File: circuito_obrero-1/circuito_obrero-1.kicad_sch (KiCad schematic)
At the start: 41 parts, among them J1 Conn_01x03_Pin, J10 Conn_01x05, J2 Conn_01x03_Pin, J3 Conn_01x03_Pin, J4 Conn_01x03_Pin, J5 Conn_01x03_Pin, J6 Conn_01x03_Pin, J7 Conn_01x03_Pin, J8 Conn_01x03_Pin, J9 Conn_01x05, U1 74HC165, U2 74HC165, U3 74HC165

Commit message: pre añadir lagrimas
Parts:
- removed H_A_j3_pin3, H_B_j3_pin3: MountingHole_Pad, MountingHole:MountingHole_2.2mm_M2_DIN965_Pad_TopOnly, symbol Mechanical:MountingHole_Pad
- added PUENTE_1, PUENTE_2, PUENTE_3, PUENTE_4, PUENTE_7, PUENTE_9: 0k, Resistor_THT:R_Axial_DIN0204_L3.6mm_D1.6mm_P7.62mm_Horizontal, symbol Device:R
- added PUENTE_5: 0k, Resistor_THT:R_Axial_DIN0207_L6.3mm_D2.5mm_P15.24mm_Horizontal, symbol Device:R
- added PUENTE_6, PUENTE_8: 0k, Resistor_THT:R_Axial_DIN0207_L6.3mm_D2.5mm_P10.16mm_Horizontal, symbol Device:R
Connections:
- net GND: now also PUENTE_6.1, PUENTE_6.2, PUENTE_7.1, PUENTE_7.2, PUENTE_8.1, PUENTE_8.2
- net VCC: now also PUENTE_9.1, PUENTE_9.2
- net at J2.1 (Pin_1), R4.2, U1.14 (D3): now also PUENTE_1.1, PUENTE_1.2
- net at J10.1 (Pin_1), J9.1 (Pin_1), U1.1 (~{PL})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: now also PUENTE_2.1, PUENTE_2.2, PUENTE_4.1, PUENTE_4.2
- net at U2.9 (Q7), U3.10 (DS): now also PUENTE_5.1, PUENTE_5.2
- net at U1.9 (Q7), U2.10 (DS): now also PUENTE_3.1, PUENTE_3.2
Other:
- moved on the sheet: H5_A_j8_pin1, R4, R9

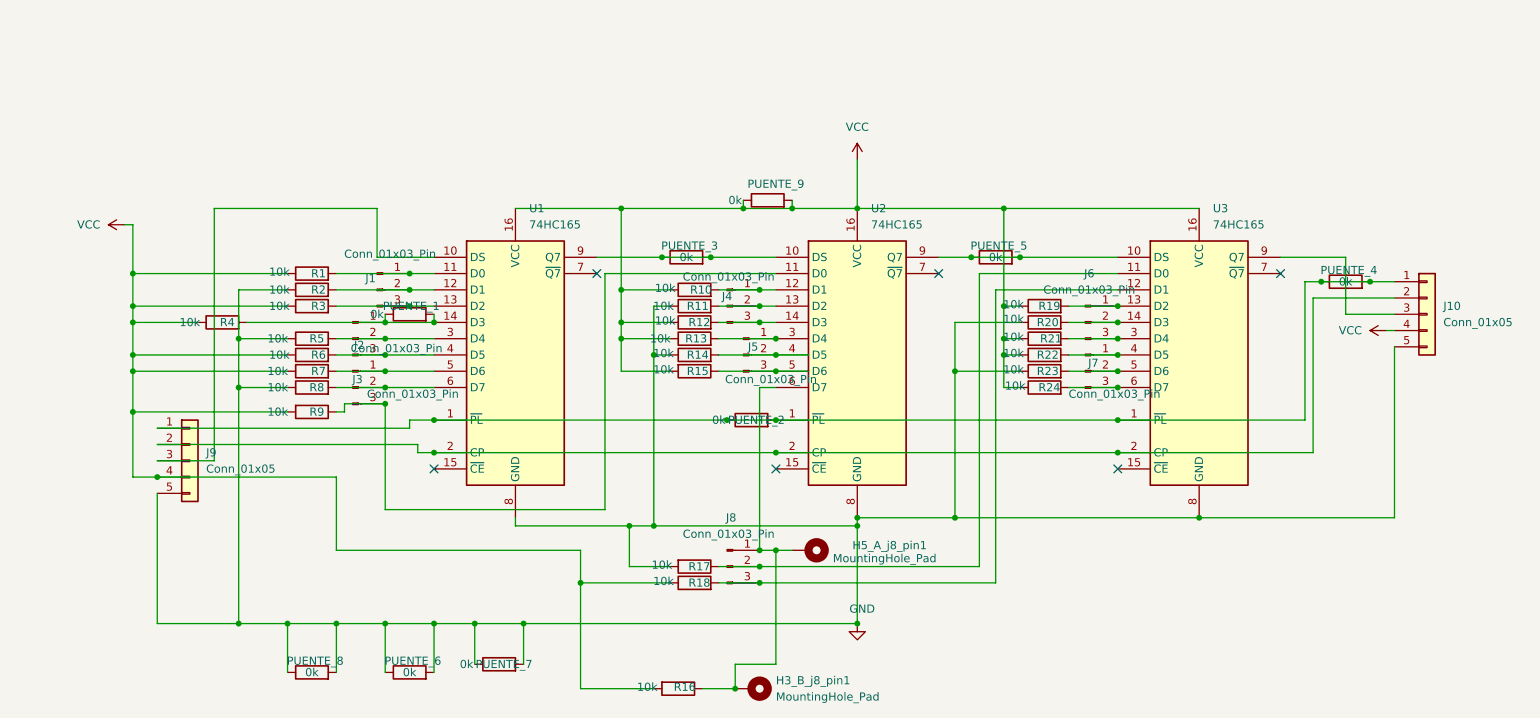
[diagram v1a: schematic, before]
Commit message: redo de circuito 2 chip x 4 encoder
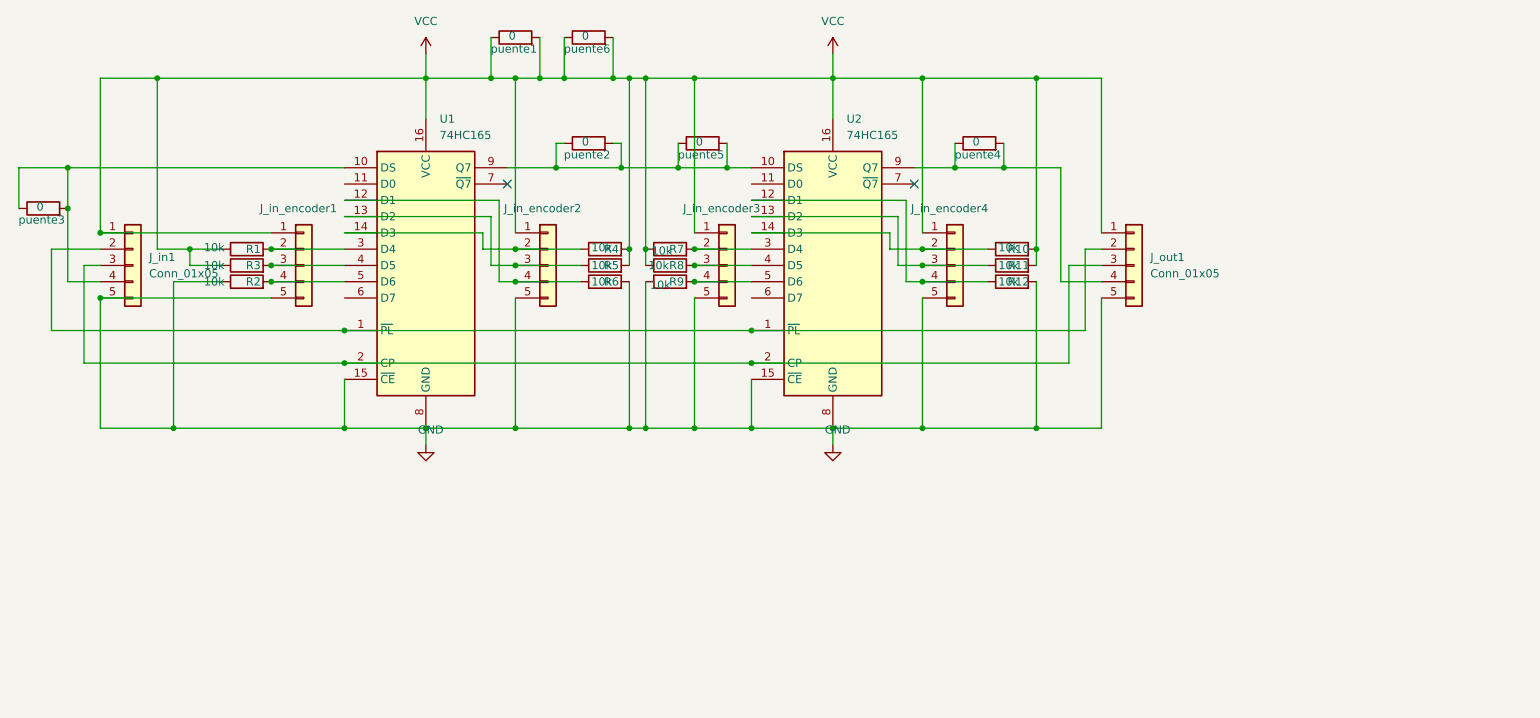
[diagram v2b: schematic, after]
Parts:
- removed H3_B_j8_pin1, H5_A_j8_pin1: MountingHole_Pad, MountingHole:MountingHole_2.2mm_M2_DIN965_Pad_TopOnly, symbol Mechanical:MountingHole_Pad
- removed J1, J2, J3, J4, J5, J6, J7, J8: Conn_01x03_Pin, Connector_JST:JST_EH_B3B-EH-A_1x03_P2.50mm_Vertical, symbol Connector:Conn_01x03_Pin
- removed PUENTE_1, PUENTE_2, PUENTE_3, PUENTE_4, PUENTE_7, PUENTE_9: 0k, Resistor_THT:R_Axial_DIN0204_L3.6mm_D1.6mm_P7.62mm_Horizontal, symbol Device:R
- removed PUENTE_5: 0k, Resistor_THT:R_Axial_DIN0207_L6.3mm_D2.5mm_P15.24mm_Horizontal, symbol Device:R
- removed PUENTE_6, PUENTE_8: 0k, Resistor_THT:R_Axial_DIN0207_L6.3mm_D2.5mm_P10.16mm_Horizontal, symbol Device:R
- removed R13, R14, R15, R16, R17, R18, R19, R20, R21, R22, R23, R24: 10k, Resistor_THT:R_Axial_DIN0204_L3.6mm_D1.6mm_P7.62mm_Horizontal, symbol Device:R
- removed U3: 74HC165, Package_DIP:CERDIP-16_W7.62mm_SideBrazed_LongPads_Socket, symbol 74xx:74HC165
- added J_in_encoder1, J_in_encoder2, J_in_encoder3, J_in_encoder4: Conn_01x05, Connector_JST:JST_EH_B5B-EH-A_1x05_P2.50mm_Vertical, symbol Connector_Generic:Conn_01x05
- added puente1, puente2, puente3, puente4, puente5, puente6: 0, Resistor_THT:R_Axial_DIN0204_L3.6mm_D1.6mm_P7.62mm_Horizontal, symbol Device:R
- renumbered J9 to J_in1, J10 to J_out1
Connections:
- net GND: now also R12.2, R6.2, R9.1, U1.15 (~{CE}), U2.15 (~{CE}), J_in_encoder1.5 (Pin_5), J_in_encoder2.5 (Pin_5), J_in_encoder3.5 (Pin_5), J_in_encoder4.5 (Pin_5); no longer R11.1, R5.1, R8.1
- net VCC: now also J_in1.1 (Pin_1), J_out1.1 (Pin_1), R10.2, R11.2, R4.2, R5.2, R8.1, J_in_encoder1.1 (Pin_1), J_in_encoder2.1 (Pin_1), J_in_encoder3.1 (Pin_1), J_in_encoder4.1 (Pin_1), puente1.1, puente1.2, puente6.1, puente6.2; no longer J_in1.4 (Pin_4), J_out1.4 (Pin_4), R10.1, R12.1, R4.1, R6.1, R9.2
- net at U2.5 (D6): now also R9.2, J_in_encoder3.4 (Pin_4)
- net at U1.13 (D2): now also R5.1, J_in_encoder2.3 (Pin_3); no longer R3.2
- net at U2.12 (D1): now also R12.1, J_in_encoder4.4 (Pin_4); no longer R10.2
- net at U2.9 (Q7): now also J_out1.4 (Pin_4), puente4.1, puente4.2
- net at R7.2: now also U2.3 (D4), J_in_encoder3.2 (Pin_2); no longer U1.5 (D6)
- net at R8.2: now also U2.4 (D5), J_in_encoder3.3 (Pin_3); no longer U1.6 (D7)
- net at U2.11 (D0): no longer R9.1
- net at R1.2: now also U1.3 (D4), J_in_encoder1.2 (Pin_2); no longer U1.11 (D0)
- net at U1.12 (D1): now also R6.1, J_in_encoder2.4 (Pin_4); no longer R2.2
- net at U1.14 (D3): now also R4.1, J_in_encoder2.2 (Pin_2); no longer R4.2
- net at U1.4 (D5): now also R3.2, J_in_encoder1.3 (Pin_3); no longer R6.2
- net at U1.1 (~{PL}), U2.1 (~{PL}): now also J_in1.2 (Pin_2), J_out1.2 (Pin_2); no longer J_in1.1 (Pin_1), J_out1.1 (Pin_1)
- net at U1.2 (CP), U2.2 (CP): now also J_in1.3 (Pin_3), J_out1.3 (Pin_3); no longer J_in1.2 (Pin_2), J_out1.2 (Pin_2)
- net at U1.9 (Q7), U2.10 (DS): now also puente2.1, puente2.2, puente5.1, puente5.2
- net at U2.14 (D3): now also R10.1, J_in_encoder4.2 (Pin_2); no longer R12.2
- net at U1.10 (DS): now also J_in1.4 (Pin_4), puente3.1, puente3.2; no longer J_in1.3 (Pin_3)
- net at U2.13 (D2): now also R11.1, J_in_encoder4.3 (Pin_3); no longer R11.2
- new net: J_in_encoder1.4 (Pin_4), R2.2, U1.5 (D6)
- no-connect marks 6 -> 2
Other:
- moved on the sheet: J_in1, J_out1, R1, R2, R3, U1

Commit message: circuito doble impresoin manual
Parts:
- added H1, H2, H3, H4: MountingHole, MountingHole:MountingHole_3.2mm_M3_DIN965, symbol Mechanical:MountingHole

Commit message: pines sueltos a gnd
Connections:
- net GND: now also U1.11 (D0), U1.6 (D7), U2.11 (D0), U2.6 (D7)
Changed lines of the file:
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@@
+	)
+	(junction
+		(at 71.12 109.22)
+		(diameter 0)
+		(color 0 0 0 0)
 	)
 	(junction
@@
 	)
 	(junction
+		(at 125.73 109.22)
+		(diameter 0)
+		(color 0 0 0 0)
+	)
+	(junction
 		(at 182.88 54.61)
 		(diameter 0)
@@
 	)
 	(junction
+		(at 133.35 109.22)
+		(diameter 0)
+		(color 0 0 0 0)
+	)
+	(junction
 		(at 138.43 93.98)
 		(diameter 0)
@@
 	(junction
 		(at 129.54 86.36)
+		(diameter 0)
+		(color 0 0 0 0)
+	)
+	(junction
+		(at 52.07 109.22)
 		(diameter 0)
 		(color 0 0 0 0)
@@
 	(wire
 		(pts
+			(xy 71.12 109.22) (xy 74.93 109.22)
+		)
+		(stroke
+			(width 0)
+			(type default)
+		)
+	)
+	(wire
+		(pts
 			(xy 45.72 54.61) (xy 87.63 54.61)
 		)
@@
 	(wire
 		(pts
+			(xy 71.12 88.9) (xy 71.12 109.22)
+		)
+		(stroke
+			(width 0)
+			(type default)
+		)
+	)
+	(wire
+		(pts
 			(xy 74.93 73.66) (xy 99.06 73.66)
 		)
@@
 	(wire
 		(pts
-			(xy 121.92 109.22) (xy 129.54 109.22)
+			(xy 121.92 109.22) (xy 125.73 109.22)
 		)
 		(stroke
@@
 	(wire
 		(pts
+			(xy 52.07 71.12) (xy 52.07 109.22)
+		)
+		(stroke
+			(width 0)
+			(type default)
+		)
+	)
+	(wire
+		(pts
 			(xy 129.54 88.9) (xy 129.54 109.22)
 		)
@@
 	(wire
 		(pts
+			(xy 74.93 71.12) (xy 52.07 71.12)
+		)
+		(stroke
+			(width 0)
+			(type default)
+		)
+	)
+	(wire
+		(pts
 			(xy 74.93 109.22) (xy 87.63 109.22)
 		)
@@
 	(wire
 		(pts
+			(xy 125.73 109.22) (xy 129.54 109.22)
+		)
+		(stroke
+			(width 0)
+			(type default)
+		)
+	)
+	(wire
+		(pts
 			(xy 170.18 64.77) (xy 170.18 68.58)
 		)
@@
 	(wire
 		(pts
+			(xy 125.73 71.12) (xy 125.73 109.22)
+		)
+		(stroke
+			(width 0)
+			(type default)
+		)
+	)
+	(wire
+		(pts
 			(xy 160.02 78.74) (xy 160.02 81.28)
 		)
@@
 	(wire
 		(pts
+			(xy 133.35 109.22) (xy 138.43 109.22)
+		)
+		(stroke
+			(width 0)
+			(type default)
+		)
+	)
+	(wire
+		(pts
 			(xy 105.41 54.61) (xy 109.22 54.61)
 		)
@@
 	(wire
 		(pts
+			(xy 52.07 109.22) (xy 71.12 109.22)
+		)
+		(stroke
+			(width 0)
+			(type default)
+		)
+	)
+	(wire
+		(pts
 			(xy 165.1 83.82) (xy 175.26 83.82)
 		)
@@
 	(wire
 		(pts
+			(xy 74.93 88.9) (xy 71.12 88.9)
+		)
+		(stroke
+			(width 0)
+			(type default)
+		)
+	)
+	(wire
+		(pts
 			(xy 29.21 81.28) (xy 36.83 81.28)
 		)
@@
 	(wire
 		(pts
+			(xy 138.43 88.9) (xy 138.43 92.71)
+		)
+		(stroke
+			(width 0)
+			(type default)
+		)
+	)
+	(wire
+		(pts
 			(xy 177.8 68.58) (xy 170.18 68.58)
 		)
@@
 	(wire
 		(pts
+			(xy 133.35 92.71) (xy 133.35 109.22)
+		)
+		(stroke
+			(width 0)
+			(type default)
+		)
+	)
+	(wire
+		(pts
 			(xy 107.95 64.77) (xy 107.95 68.58)
 		)
@@
 	(wire
 		(pts
-			(xy 129.54 109.22) (xy 138.43 109.22)
+			(xy 129.54 109.22) (xy 133.35 109.22)
+		)
+		(stroke
+			(width 0)
+			(type default)
+		)
+	)
+	(wire
+		(pts
+			(xy 138.43 92.71) (xy 133.35 92.71)
 		)
 		(stroke
@@
 	(wire
 		(pts
-			(xy 48.26 109.22) (xy 74.93 109.22)
+			(xy 48.26 109.22) (xy 52.07 109.22)
 		)
 		(stroke
@@
 		)
 		(stroke
+			(width 0)
+			(type default)
+		)
+	)
+	(wire
+		(pts
+			(xy 138.43 71.12) (xy 125.73 71.12)
+		)
+		(stroke
